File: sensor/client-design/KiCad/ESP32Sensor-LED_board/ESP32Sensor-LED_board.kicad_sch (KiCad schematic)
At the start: 48 parts, among them J1 CLP-103-02-F-D-BE, J2 CLP-103-02-F-D-BE, K1 IRLHS6376TRPBF, K2 IRLHS6376TRPBF, U1 TL4242TDRJRQ1, U2 TL4242TDRJRQ1, U3 TL4242TDRJRQ1, U4 TL4242TDRJRQ1, U5 VL53L0CXV0DH/1

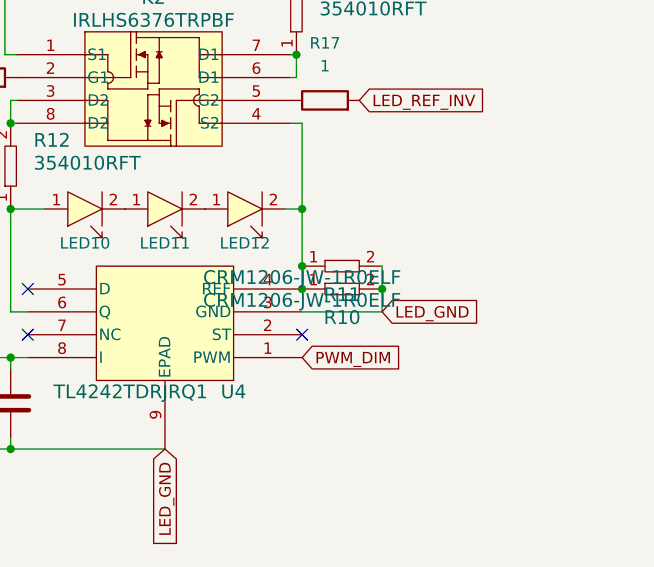
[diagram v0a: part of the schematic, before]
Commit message: Move sensor PCB to center
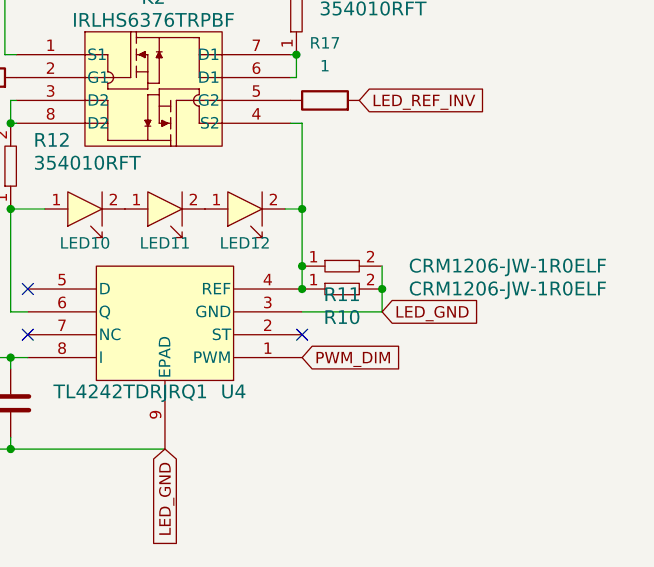
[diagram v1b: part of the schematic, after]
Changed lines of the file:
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@@
       (effects (font (size 1.524 1.524)))
     )
-    (property "Value" "CRM1206-JW-1R0ELF" (at 205.105 113.665 0)
+    (property "Value" "CRM1206-JW-1R0ELF" (at 227.965 112.395 0)
       (effects (font (size 1.524 1.524)))
     )
@@
       (effects (font (size 1.524 1.524)))
     )
-    (property "Value" "CRM1206-JW-1R0ELF" (at 205.105 116.205 0)
-      (effects (font (size 1.524 1.524)))
-    )
+    (property "Value" "CRM1206-JW-1R0ELF" (at 227.965 114.935 0)
+      (effects (font (size 1.524 1.524)))
+    )
